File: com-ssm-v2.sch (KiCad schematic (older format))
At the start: 23 parts, among them J1 RST_JMP, J2 DEBUG CONN, J3 PROGRAMMING PORT, P1 CONN_02X10, P2 CONN_02X10, SW1 SW_RST, U1 SN65HVD230, U2 ATMEGA32M1-MU, Y1 8MHz

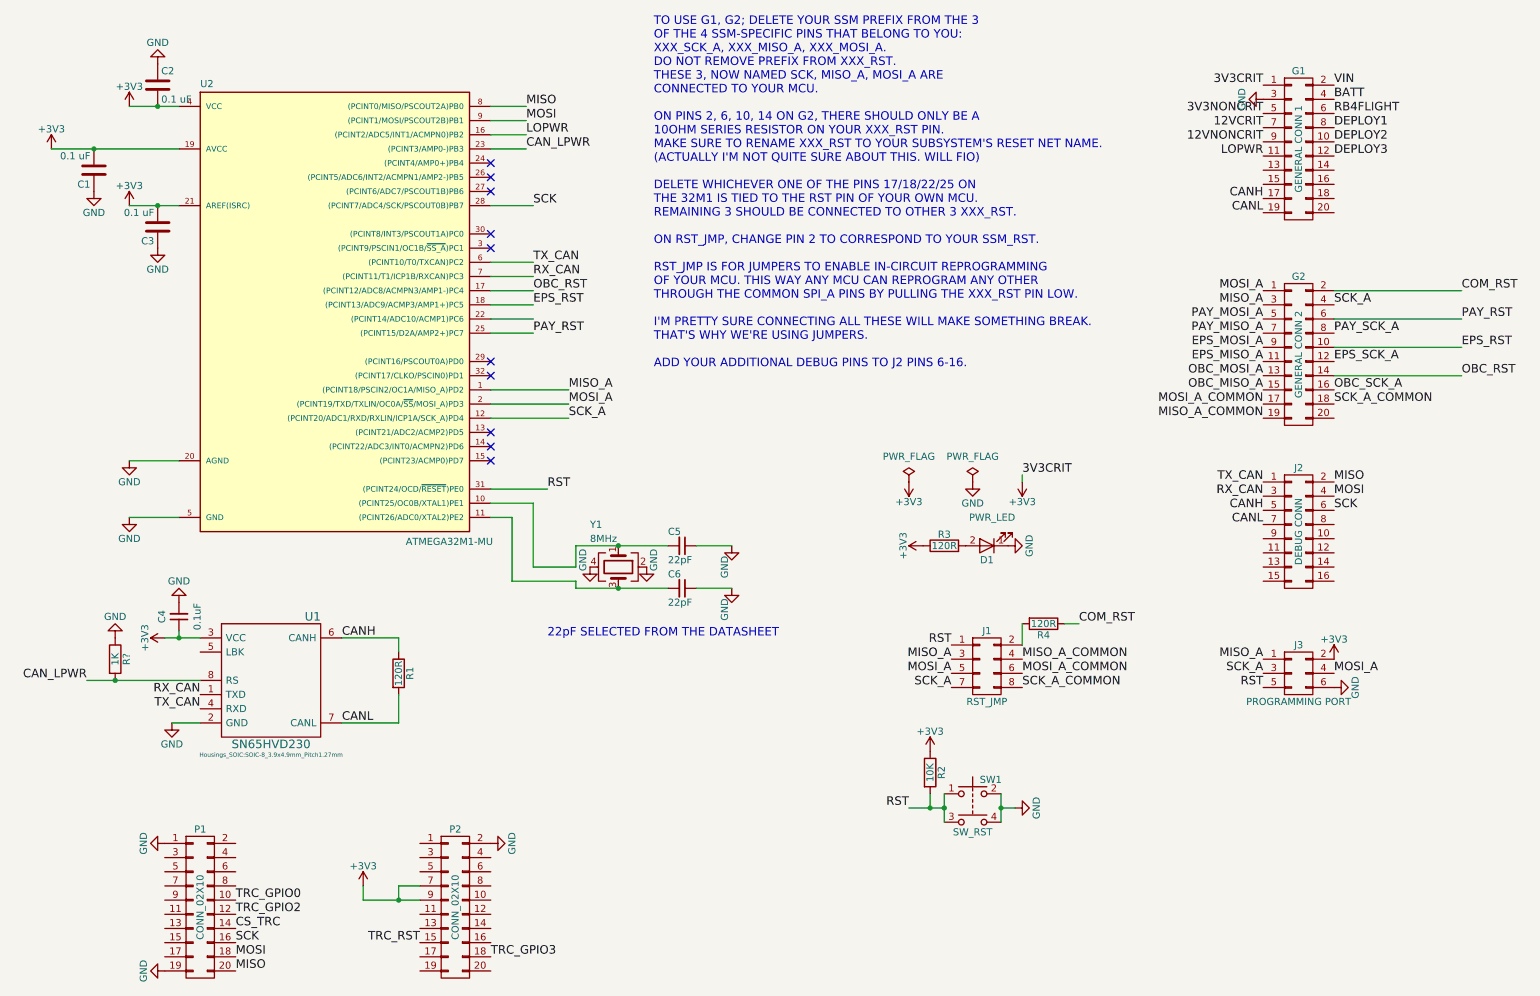
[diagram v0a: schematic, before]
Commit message: COM board layout
Added headers for cc1120 module. added reference files for cc1120 module
pcb
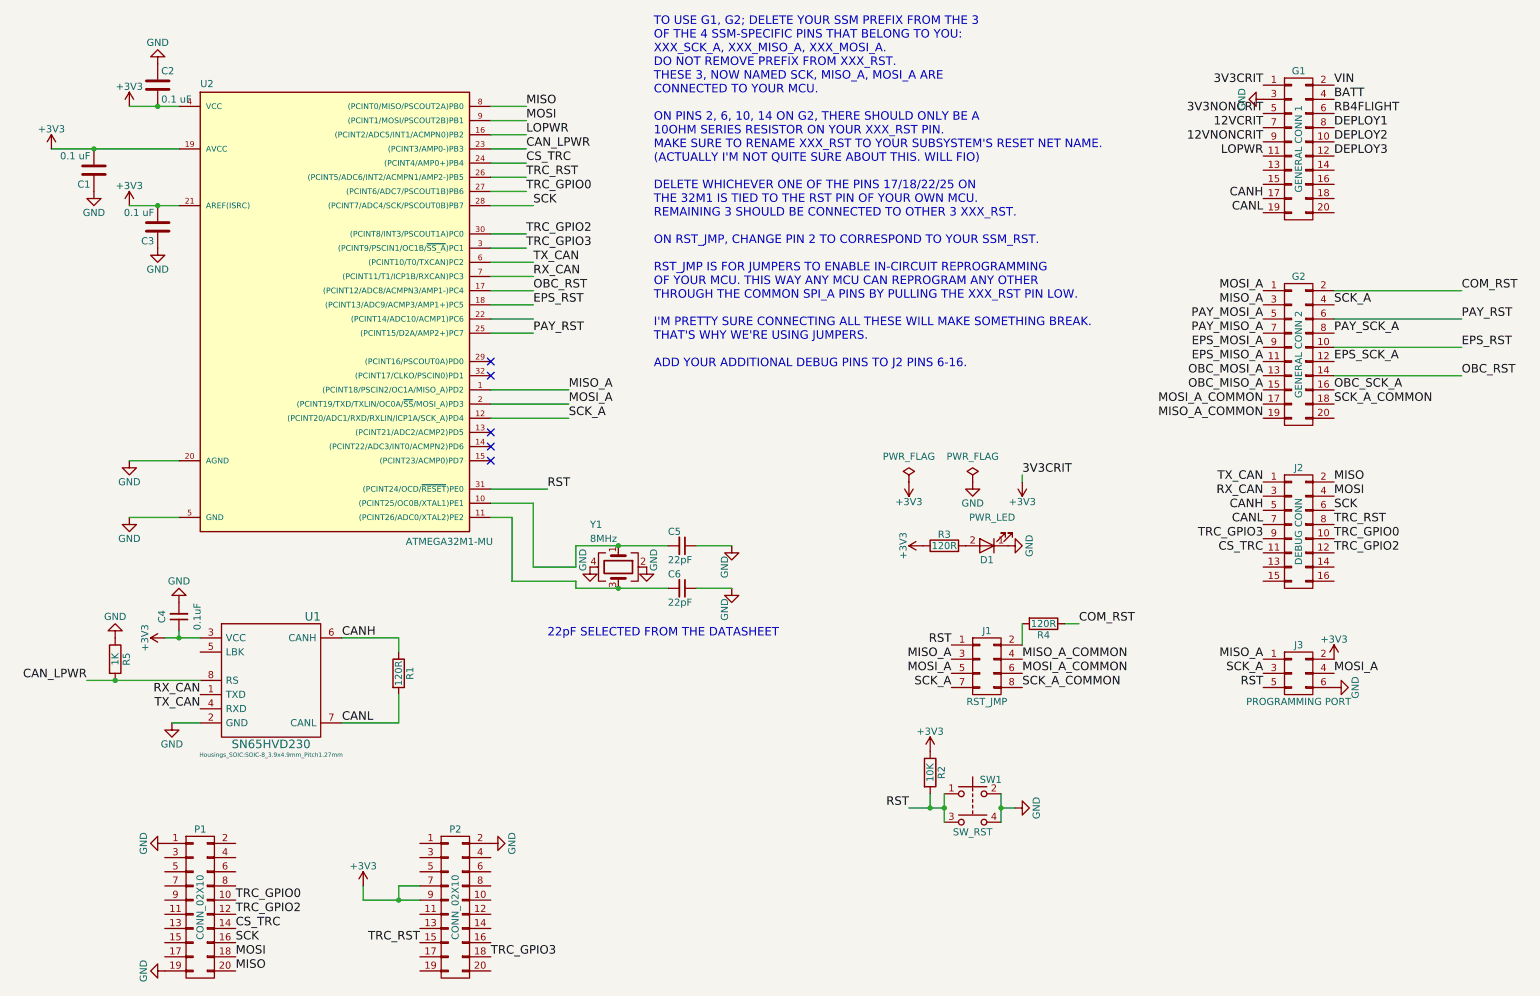
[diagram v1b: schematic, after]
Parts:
- P1, P2: footprint (none) -> Socket_Strips:Socket_Strip_Straight_2x10_Pitch1.27mm
- gave numbers to parts that had none: 1
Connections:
- net CS_TRC: now also J2.11 (P11), U2.24 ((PCINT4/AMP0+)PB4)
- net TRC_GPIO0: now also J2.10 (P10), U2.27 ((PCINT6/ADC7/PSCOUT1B)PB6)
- net TRC_GPIO2: now also J2.12 (P12), U2.30 ((PCINT8/INT3/PSCOUT1A)PC0)
- net TRC_GPIO3: now also J2.9 (P9), U2.3 ((PCINT9/PSCIN1/OC1B/~SS_A~)PC1)
- net TRC_RST: now also J2.8 (P8), U2.26 ((PCINT5/ADC6/INT2/ACMPN1/AMP2-)PB5)
- no-connect marks 10 -> 5
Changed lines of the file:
@@
 LIBS:general_ssm
 LIBS:SN65HVD233D
+LIBS:com-ssm-v2-cache
 EELAYER 25 0
 EELAYER END
@@
 NoConn ~ 3750 3250
 NoConn ~ 3750 3150
-NoConn ~ 3750 2350
-NoConn ~ 3750 2250
 Text Label 4050 2050 0    60   ~ 0
 SCK
-NoConn ~ 3750 1950
-NoConn ~ 3750 1850
-NoConn ~ 3750 1750
 Text Label 4000 1350 0    60   ~ 0
 MISO
@@
 $EndComp
 $Comp
-L GND #PWR011
+L GND #PWR010
 U 1 1 594EEF68
 P 1500 5700
-F 0 "#PWR011" H 1500 5450 50  0001 C CNN
+F 0 "#PWR010" H 1500 5450 50  0001 C CNN
 F 1 "GND" H 1500 5550 50  0000 C CNN
 F 2 "" H 1500 5700 50  0000 C CNN
@@
 $EndComp
 $Comp
-L GND #PWR012
+L GND #PWR011
 U 1 1 594EF100
 P 1200 4250
-F 0 "#PWR012" H 1200 4000 50  0001 C CNN
+F 0 "#PWR011" H 1200 4000 50  0001 C CNN
 F 1 "GND" H 1200 4100 50  0000 C CNN
 F 2 "" H 1200 4250 50  0000 C CNN
@@
 $EndComp
 $Comp
-L GND #PWR013
+L GND #PWR012
 U 1 1 594EF3C8
 P 1200 3850
-F 0 "#PWR013" H 1200 3600 50  0001 C CNN
+F 0 "#PWR012" H 1200 3600 50  0001 C CNN
 F 1 "GND" H 1200 3700 50  0000 C CNN
 F 2 "" H 1200 3850 50  0000 C CNN
@@
 $EndComp
 $Comp
-L PWR_FLAG #FLG014
+L PWR_FLAG #FLG013
 U 1 1 594EDD5D
 P 6700 4000
-F 0 "#FLG014" H 6700 4095 50  0001 C CNN
+F 0 "#FLG013" H 6700 4095 50  0001 C CNN
 F 1 "PWR_FLAG" H 6700 4180 50  0000 C CNN
 F 2 "" H 6700 4000 50  0000 C CNN
@@
 $EndComp
 $Comp
-L +3V3 #PWR015
+L +3V3 #PWR014
 U 1 1 594EDD8C
 P 6700 4000
-F 0 "#PWR015" H 6700 3850 50  0001 C CNN
+F 0 "#PWR014" H 6700 3850 50  0001 C CNN
 F 1 "+3V3" H 6700 4140 50  0000 C CNN
 F 2 "" H 6700 4000 50  0000 C CNN
@@
 $EndComp
 $Comp
-L PWR_FLAG #FLG016
+L PWR_FLAG #FLG015
 U 1 1 594EDDFD
 P 7150 4000
-F 0 "#FLG016" H 7150 4095 50  0001 C CNN
+F 0 "#FLG015" H 7150 4095 50  0001 C CNN
 F 1 "PWR_FLAG" H 7150 4180 50  0000 C CNN
 F 2 "" H 7150 4000 50  0000 C CNN
@@
 $EndComp
 $Comp
-L GND #PWR017
+L GND #PWR016
 U 1 1 594EDE2C
 P 7150 4000
-F 0 "#PWR017" H 7150 3750 50  0001 C CNN
+F 0 "#PWR016" H 7150 3750 50  0001 C CNN
 F 1 "GND" H 7150 3850 50  0000 C CNN
 F 2 "" H 7150 4000 50  0000 C CNN
@@
 $EndComp
 $Comp
-L GND #PWR018
+L GND #PWR017
 U 1 1 598FE060
 P 9200 1300
-F 0 "#PWR018" H 9200 1050 50  0001 C CNN
+F 0 "#PWR017" H 9200 1050 50  0001 C CNN
 F 1 "GND" H 9200 1150 50  0000 C CNN
 F 2 "" H 9200 1300 50  0001 C CNN
@@
 $EndComp
 $Comp
-L GND #PWR019
+L GND #PWR018
 U 1 1 598FFC7D
 P 1400 1050
-F 0 "#PWR019" H 1400 800 50  0001 C CNN
+F 0 "#PWR018" H 1400 800 50  0001 C CNN
 F 1 "GND" H 1400 900 50  0000 C CNN
 F 2 "" H 1400 1050 50  0001 C CNN
@@
 $EndComp
 $Comp
-L GND #PWR020
+L GND #PWR019
 U 1 1 598FFDBB
 P 950 1950
-F 0 "#PWR020" H 950 1700 50  0001 C CNN
+F 0 "#PWR019" H 950 1700 50  0001 C CNN
 F 1 "GND" H 950 1800 50  0000 C CNN
 F 2 "" H 950 1950 50  0001 C CNN
@@
 $EndComp
 $Comp
-L GND #PWR021
+L GND #PWR020
 U 1 1 598FFFFF
 P 1400 2350
-F 0 "#PWR021" H 1400 2100 50  0001 C CNN
+F 0 "#PWR020" H 1400 2100 50  0001 C CNN
 F 1 "GND" H 1400 2200 50  0000 C CNN
 F 2 "" H 1400 2350 50  0001 C CNN
@@
 TO USE G1, G2; DELETE YOUR SSM PREFIX FROM THE 3 \nOF THE 4 SSM-SPECIFIC PINS THAT BELONG TO YOU:\nXXX_SCK_A, XXX_MISO_A, XXX_MOSI_A. \nDO NOT REMOVE PREFIX FROM XXX_RST.\nTHESE 3, NOW NAMED SCK, MISO_A, MOSI_A ARE\nCONNECTED TO YOUR MCU.\n\nON PINS 2, 6, 10, 14 ON G2, THERE SHOULD ONLY BE A\n10OHM SERIES RESISTOR ON YOUR XXX_RST PIN. \nMAKE SURE TO RENAME XXX_RST TO YOUR SUBSYSTEM'S RESET NET NAME.\n(ACTUALLY I'M NOT QUITE SURE ABOUT THIS. WILL FIO)\n\nDELETE WHICHEVER ONE OF THE PINS 17/18/22/25 ON \nTHE 32M1 IS TIED TO THE RST PIN OF YOUR OWN MCU. \nREMAINING 3 SHOULD BE CONNECTED TO OTHER 3 XXX_RST.\n \nON RST_JMP, CHANGE PIN 2 TO CORRESPOND TO YOUR SSM_RST.\n\nRST_JMP IS FOR JUMPERS TO ENABLE IN-CIRCUIT REPROGRAMMING \nOF YOUR MCU. THIS WAY ANY MCU CAN REPROGRAM ANY OTHER \nTHROUGH THE COMMON SPI_A PINS BY PULLING THE XXX_RST PIN LOW.\n\nI'M PRETTY SURE CONNECTING ALL THESE WILL MAKE SOMETHING BREAK.\nTHAT'S WHY WE'RE USING JUMPERS.\n\nADD YOUR ADDITIONAL DEBUG PINS TO J2 PINS 6-16.
 $Comp
-L +3V3 #PWR022
+L +3V3 #PWR021
 U 1 1 598FF9DC
 P 7500 4000
-F 0 "#PWR022" H 7500 3850 50  0001 C CNN
+F 0 "#PWR021" H 7500 3850 50  0001 C CNN
 F 1 "+3V3" H 7500 4140 50  0000 C CNN
 F 2 "" H 7500 4000 50  0000 C CNN
@@
 $EndComp
 $Comp
-L GND #PWR023
+L GND #PWR022
 U 1 1 598FFE1E
 P 4850 4600
-F 0 "#PWR023" H 4850 4350 50  0001 C CNN
+F 0 "#PWR022" H 4850 4350 50  0001 C CNN
 F 1 "GND" V 4900 4650 50  0000 C CNN
 F 2 "" H 4850 4600 50  0001 C CNN
@@
 $EndComp
 $Comp
-L GND #PWR024
+L GND #PWR023
 U 1 1 598FFEB9
 P 4450 4600
-F 0 "#PWR024" H 4450 4350 50  0001 C CNN
+F 0 "#PWR023" H 4450 4350 50  0001 C CNN
 F 1 "GND" V 4400 4650 50  0000 C CNN
 F 2 "" H 4450 4600 50  0001 C CNN
@@
 $EndComp
 $Comp
-L +3V3 #PWR025
+L +3V3 #PWR024
 U 1 1 59903496
 P 6800 4450
-F 0 "#PWR025" H 6800 4300 50  0001 C CNN
+F 0 "#PWR024" H 6800 4300 50  0001 C CNN
 F 1 "+3V3" H 6800 4590 50  0000 C CNN
 F 2 "" H 6800 4450 50  0000 C CNN
@@
 $EndComp
 $Comp
-L GND #PWR026
+L GND #PWR025
 U 1 1 599034E6
 P 7400 4450
-F 0 "#PWR026" H 7400 4200 50  0001 C CNN
+F 0 "#PWR025" H 7400 4200 50  0001 C CNN
 F 1 "GND" H 7400 4300 50  0000 C CNN
 F 2 "" H 7400 4450 50  0000 C CNN
@@
 	7350 6200 7350 6400
 $Comp
-L GND #PWR027
+L GND #PWR026
 U 1 1 59907B9F
 P 7450 6300
-F 0 "#PWR027" H 7450 6050 50  0001 C CNN
+F 0 "#PWR026" H 7450 6050 50  0001 C CNN
 F 1 "GND" H 7450 6150 50  0000 C CNN
 F 2 "" H 7450 6300 50  0000 C CNN
@@
 $EndComp
 $Comp
-L +3V3 #PWR028
+L +3V3 #PWR027
 U 1 1 599089D2
 P 6850 5900
-F 0 "#PWR028" H 6850 5750 50  0001 C CNN
+F 0 "#PWR027" H 6850 5750 50  0001 C CNN
 F 1 "+3V3" H 6850 6040 50  0000 C CNN
 F 2 "" H 6850 5900 50  0000 C CNN
@@
 	3750 1650 4000 1650
 $Comp
-L R R?
+L R R5
 U 1 1 59973E79
 P 1100 5250
-F 0 "R?" V 1180 5250 50  0000 C CNN
+F 0 "R5" V 1180 5250 50  0000 C CNN
 F 1 "1K" V 1100 5250 50  0000 C CNN
 F 2 "Resistors_SMD:R_0603" V 1030 5250 50  0001 C CNN
@@
 $EndComp
 $Comp
-L GND #PWR010
+L GND #PWR028
 U 1 1 594EEA8D
 P 1100 5100
-F 0 "#PWR010" H 1100 4850 50  0001 C CNN
+F 0 "#PWR028" H 1100 4850 50  0001 C CNN
 F 1 "GND" H 1100 4950 50  0000 C CNN
 F 2 "" H 1100 5100 50  0000 C CNN
@@
 $EndComp
 $Comp
-L ATMEGA32M1-MU U2
-U 1 1 59464C0C
-P 2650 3050
-F 0 "U2" H 1700 4880 50  0000 L BNN
-F 1 "ATMEGA32M1-MU" H 3150 1650 50  0000 L BNN
-F 2 "Housings_QFP:TQFP-32_7x7mm_Pitch0.8mm" H 2650 3050 50  0001 C CIN
-F 3 "" H 2650 3050 50  0001 C CNN
-	1    2650 3050
-	1    0    0    -1
-$EndComp
-$Comp
 L CONN_02X10 P1
 U 1 1 59973AEC
@@
 F 0 "P1" H 1700 7550 50  0000 C CNN
 F 1 "CONN_02X10" V 1700 7000 50  0000 C CNN
-F 2 "" H 1700 5800 50  0001 C CNN
+F 2 "Socket_Strips:Socket_Strip_Straight_2x10_Pitch1.27mm" H 1700 5800 50  0001 C CNN
 F 3 "" H 1700 5800 50  0001 C CNN
 	1    1700 7000
@@
 F 0 "P2" H 3500 7550 50  0000 C CNN
 F 1 "CONN_02X10" V 3500 7000 50  0000 C CNN
-F 2 "" H 3500 5800 50  0001 C CNN
+F 2 "Socket_Strips:Socket_Strip_Straight_2x10_Pitch1.27mm" H 3500 5800 50  0001 C CNN
 F 3 "" H 3500 5800 50  0001 C CNN
 	1    3500 7000
@@
 MISO
 $Comp
-L GND #PWR?
+L GND #PWR029
 U 1 1 59974102
 P 1450 7450
-F 0 "#PWR?" H 1450 7200 50  0001 C CNN
+F 0 "#PWR029" H 1450 7200 50  0001 C CNN
 F 1 "GND" H 1450 7300 50  0000 C CNN
 F 2 "" H 1450 7450 50  0000 C CNN
@@
 $EndComp
 $Comp
-L GND #PWR?
+L GND #PWR030
 U 1 1 5997419D
 P 1450 6550
-F 0 "#PWR?" H 1450 6300 50  0001 C CNN
+F 0 "#PWR030" H 1450 6300 50  0001 C CNN
 F 1 "GND" H 1450 6400 50  0000 C CNN
 F 2 "" H 1450 6550 50  0000 C CNN
@@
 TRC_GPIO3
 $Comp
-L GND #PWR?
+L GND #PWR031
 U 1 1 599743D9
 P 3750 6550
-F 0 "#PWR?" H 3750 6300 50  0001 C CNN
+F 0 "#PWR031" H 3750 6300 50  0001 C CNN
 F 1 "GND" H 3750 6400 50  0000 C CNN
 F 2 "" H 3750 6550 50  0000 C CNN
@@
 $EndComp
 $Comp
-L +3V3 #PWR?
+L +3V3 #PWR032
 U 1 1 59974587
 P 2850 6850
-F 0 "#PWR?" H 2850 6700 50  0001 C CNN
+F 0 "#PWR032" H 2850 6700 50  0001 C CNN
 F 1 "+3V3" H 2850 6990 50  0000 C CNN
 F 2 "" H 2850 6850 50  0000 C CNN
@@
 	2850 6950 2850 6850
 Connection ~ 3100 6950
+Text Label 4000 1750 0    60   ~ 0
+CS_TRC
+Wire Wire Line
+	3750 1750 4000 1750
+Wire Wire Line
+	3750 1850 4000 1850
+Text Label 4000 1850 0    60   ~ 0
+TRC_RST
+Wire Wire Line
+	3750 1950 4000 1950
+Text Label 4000 1950 0    60   ~ 0
+TRC_GPIO0
+$Comp
+L ATMEGA32M1-MU U2
+U 1 1 59464C0C
+P 2650 3050
+F 0 "U2" H 1700 4880 50  0000 L BNN
+F 1 "ATMEGA32M1-MU" H 3150 1650 50  0000 L BNN
+F 2 "Housings_QFP:TQFP-32_7x7mm_Pitch0.8mm" H 2650 3050 50  0001 C CIN
+F 3 "" H 2650 3050 50  0001 C CNN
+	1    2650 3050
+	1    0    0    -1
+$EndComp
+Wire Wire Line
+	3750 2250 4000 2250
+Wire Wire Line
+	3750 2350 4000 2350
+Text Label 4000 2250 0    60   ~ 0
+TRC_GPIO2
+Text Label 4000 2350 0    60   ~ 0
+TRC_GPIO3
+Text Label 9700 4300 0    60   ~ 0
+TRC_RST
+Text Label 9700 4400 0    60   ~ 0
+TRC_GPIO0
+Text Label 9700 4500 0    60   ~ 0
+TRC_GPIO2
+Text Label 9200 4400 2    60   ~ 0
+TRC_GPIO3
+Text Label 9200 4500 2    60   ~ 0
+CS_TRC
 $EndSCHEMATC
